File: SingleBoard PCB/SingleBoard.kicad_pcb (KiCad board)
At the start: 2 copper layers, 151 x 103 mm, 41 parts, among them SW1 SW_Push_45deg, SW10 SW_Push_45deg, SW11 SW_Push_45deg, SW12 SW_Push_45deg, SW13 SW_Push_45deg, SW14 SW_Push_45deg, SW15 SW_Push_45deg, SW16 SW_Push_45deg, SW17 SW_Push_45deg, SW18 SW_Push_45deg, SW19 SW_Push_45deg, SW2 SW_Push_45deg, SW3 SW_Push_45deg, SW4 SW_Push_45deg, SW5 SW_Push_45deg, SW6 SW_Push_45deg, SW7 SW_Push_45deg, SW8 SW_Push_45deg, SW9 SW_Push_45deg, U2 Seeed Studio XIAO RP2040

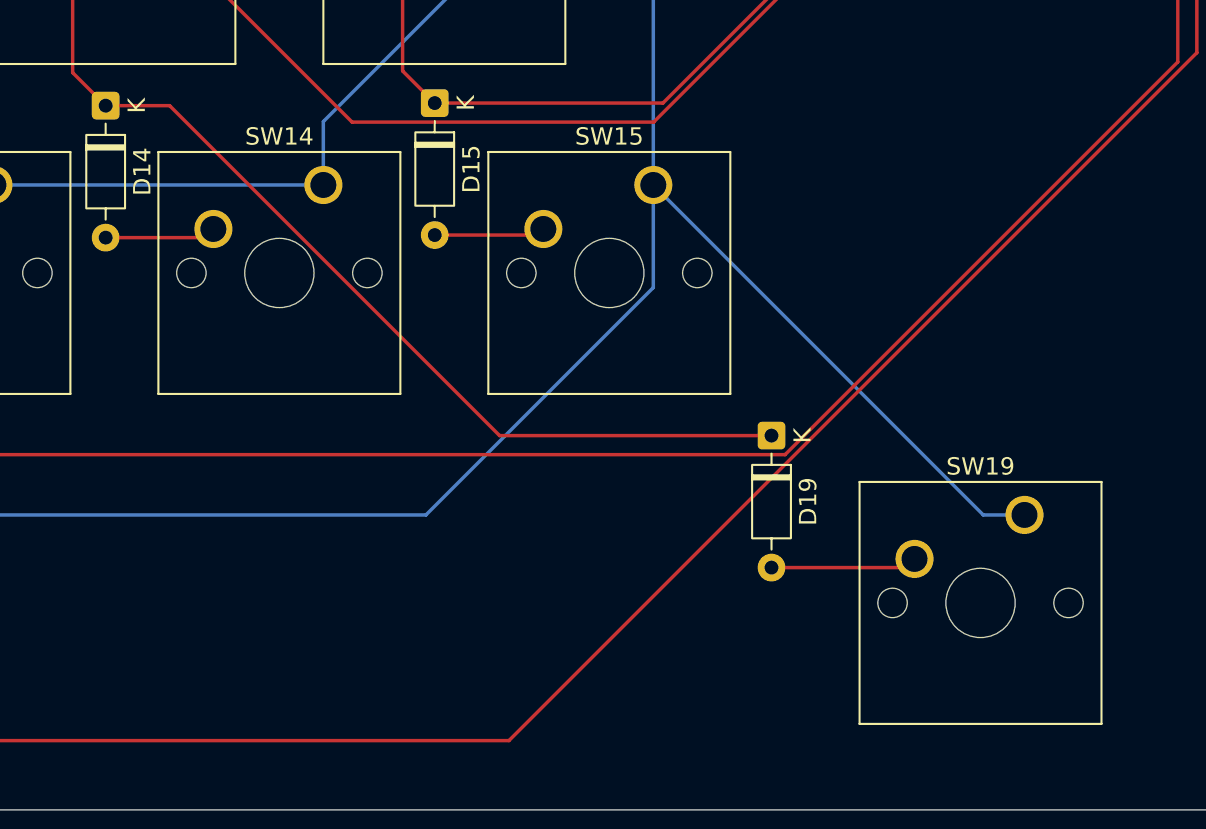
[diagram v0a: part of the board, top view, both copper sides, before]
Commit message: Made changes to case design and spacebar placement.
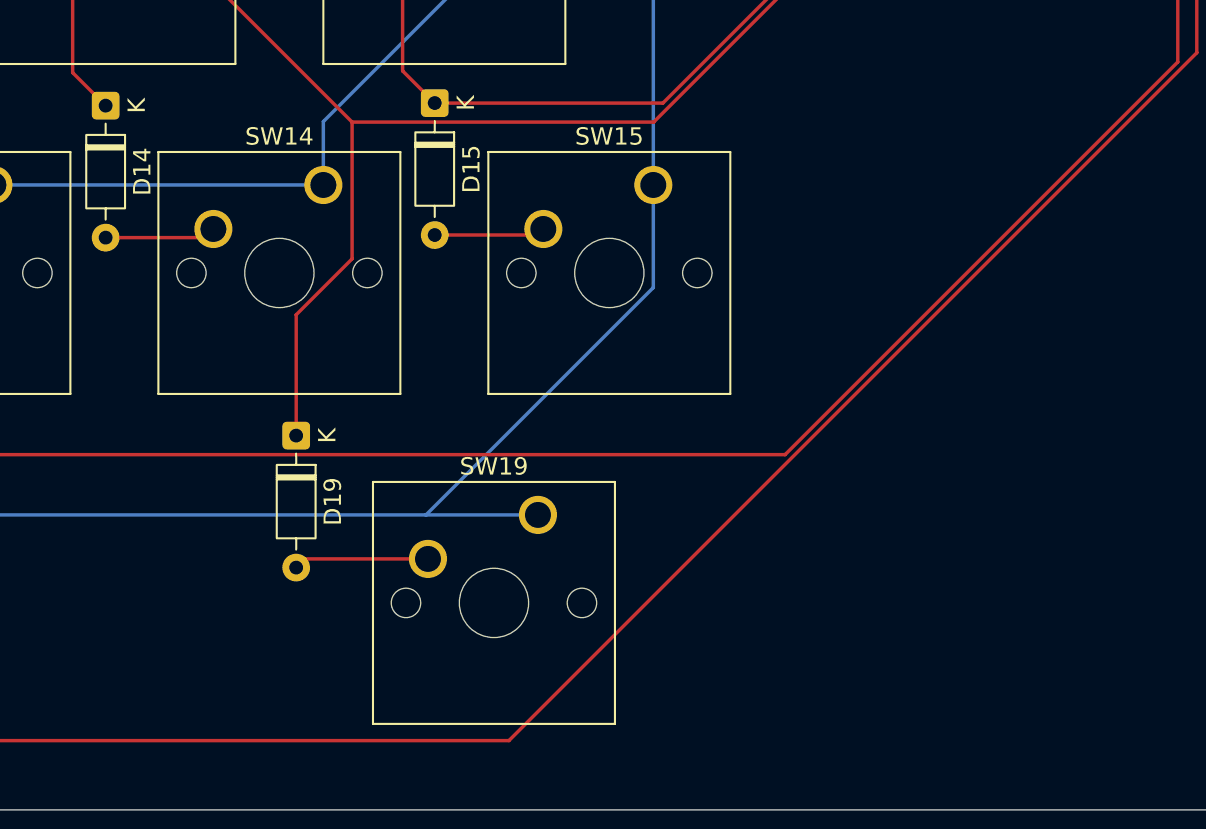
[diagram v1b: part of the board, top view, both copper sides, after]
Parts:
- moved SW19 28.1 mm to (188.0, 136.0)
- moved D19 27.4 mm to (174.0, 131.4)
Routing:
- net ROW4: track 216.5 -> 189.6 mm
- net Column3: track 197.8 -> 175.0 mm
- net Net-(D19-A): track 8.46 -> 7.82 mm
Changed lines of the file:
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@@
 			(crossoutdnponfab yes)
 			(subtractmaskfromsilk no)
-			(outputformat 3)
+			(outputformat 1)
 			(mirror no)
 			(drillshape 0)
 			(scaleselection 1)
-			(outputdirectory "C:/Users/bobby/Downloads/")
+			(outputdirectory "C:/Users/bobby/Documents/SingleBoard/Production/PCB/")
 		)
 	)
@@
 	(footprint "Diode_THT:D_DO-35_SOD27_P7.62mm_Horizontal"
 		(layer "F.Cu")
-		(at 201.44375 131.39 -90)
+		(at 174 131.39 -90)
 		(descr "Diode, DO-35_SOD27 series, Axial, Horizontal, pin pitch=7.62mm, length*diameter=4*2mm^2, http://www.diodes.com/_files/packages/DO-35.pdf")
 		(tags "Diode DO-35_SOD27 series Axial Horizontal pin pitch 7.62mm  length 4mm diameter 2mm")
@@
 	(footprint "Button_Switch_Keyboard:SW_Cherry_MX_1.00u_PCB"
 		(layer "F.Cu")
-		(at 216.05125 135.97)
+		(at 187.96 135.97)
 		(descr "Cherry MX keyswitch, 1.00u, PCB mount, http://cherryamericas.com/wp-content/uploads/2014/12/mx_cat.pdf")
 		(tags "Cherry MX keyswitch 1.00u PCB")
@@
 	)
 	(segment
-		(start 201.44375 131.39)
-		(end 185.743402 131.39)
+		(start 174 131.39)
+		(end 174 124.412944)
 		(width 0.2)
 		(layer "F.Cu")
@@
 	)
 	(segment
-		(start 154 93.19)
-		(end 157.127944 93.19)
+		(start 174 124.412944)
+		(end 177.227944 121.185)
 		(width 0.2)
 		(layer "F.Cu")
@@
 	)
 	(segment
-		(start 223 75.19)
-		(end 210.0075 75.19)
+		(start 177.227944 121.185)
+		(end 177.227944 113.29)
 		(width 0.2)
 		(layer "F.Cu")
@@
 	)
 	(segment
-		(start 185.743402 131.39)
-		(end 166.693402 112.34)
+		(start 154 93.19)
+		(end 157.127944 93.19)
 		(width 0.2)
 		(layer "F.Cu")
@@
 	)
 	(segment
-		(start 166.693402 112.34)
-		(end 163 112.34)
+		(start 223 75.19)
+		(end 210.0075 75.19)
 		(width 0.2)
 		(layer "F.Cu")
@@
 	)
 	(segment
-		(start 201.44375 139.01)
-		(end 209.20125 139.01)
+		(start 174.5 138.51)
+		(end 174 139.01)
 		(width 0.2)
 		(layer "F.Cu")
@@
 	)
 	(segment
-		(start 209.20125 139.01)
-		(end 209.70125 138.51)
+		(start 181.61 138.51)
+		(end 174.5 138.51)
 		(width 0.2)
 		(layer "F.Cu")
@@
 	)
 	(segment
-		(start 213.67 135.97)
-		(end 216.05125 135.97)
-		(width 0.2)
-		(layer "B.Cu")
-		(net 27)
-	)
-	(segment
-		(start 194.62 116.92)
-		(end 213.67 135.97)
+		(start 187.96 135.97)
+		(end 181.492944 135.97)
 		(width 0.2)
 		(layer "B.Cu")
